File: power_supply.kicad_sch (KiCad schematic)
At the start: 18 parts, among them J1 Разъём к автомобилю 2x16 (32 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, U6 MC78M05CDTG, U7 AMS1117-3.3

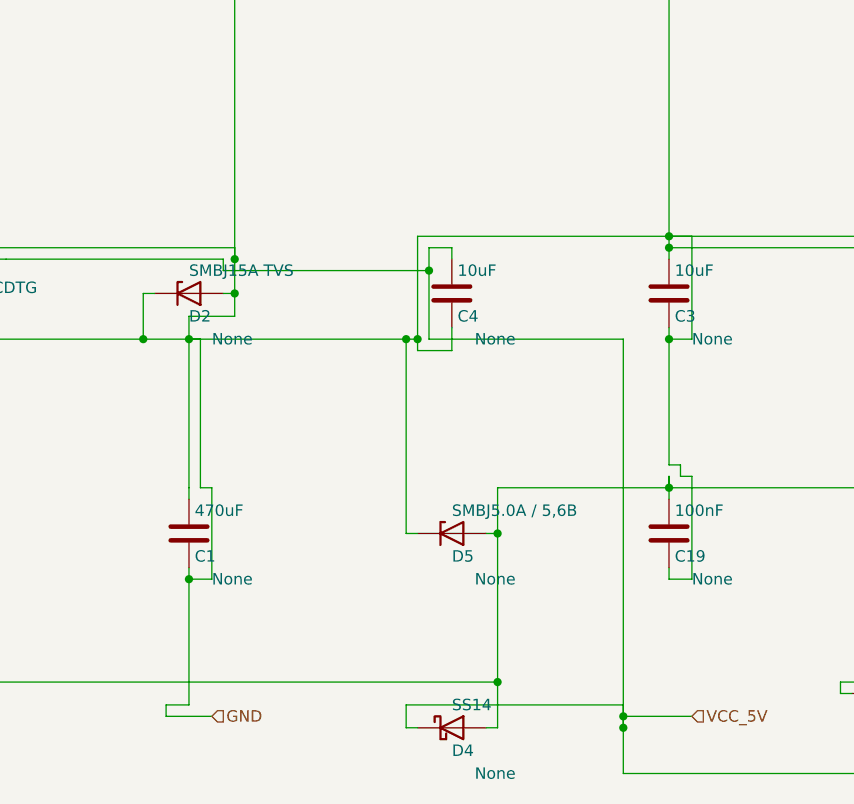
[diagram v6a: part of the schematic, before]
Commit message: фильтр клеток для Т если там пересечение
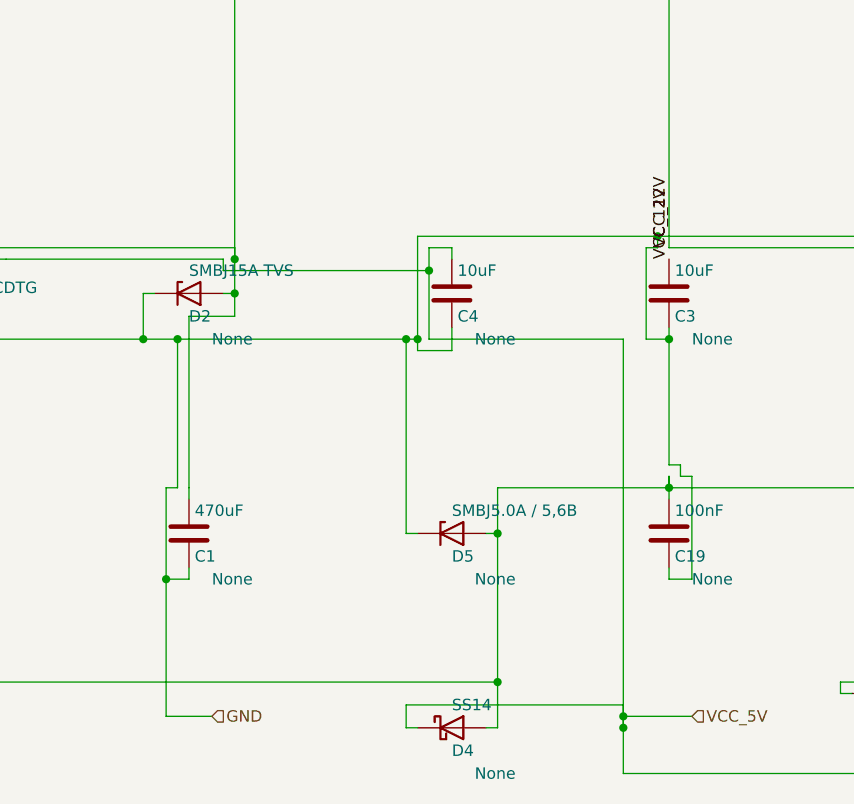
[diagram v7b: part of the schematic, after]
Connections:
- net GND: no longer C1.1, C11.1, C2.1, C20.1, C3.1, D2.2 (A), L1.2, U6.1 (VI)
- new net VCC_12V: C1.1, C11.1, C2.1, C20.1, C3.1, D2.2 (A), L1.2, U6.1 (VI)
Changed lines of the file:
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@@
 		(instances
 			(project "Untitled"
-				(path "/ddde2adb-c5de-407b-b4a5-5687a14e8471"
+				(path "/6a57f7b9-87d0-4bec-9f96-e75792a987b4"
 					(reference "C1")
 					(unit 1)
@@
 		(instances
 			(project "Untitled"
-				(path "/ddde2adb-c5de-407b-b4a5-5687a14e8471"
+				(path "/6a57f7b9-87d0-4bec-9f96-e75792a987b4"
 					(reference "C11")
 					(unit 1)
@@
 		(instances
 			(project "Untitled"
-				(path "/ddde2adb-c5de-407b-b4a5-5687a14e8471"
+				(path "/6a57f7b9-87d0-4bec-9f96-e75792a987b4"
 					(reference "C16")
 					(unit 1)
@@
 		(instances
 			(project "Untitled"
-				(path "/ddde2adb-c5de-407b-b4a5-5687a14e8471"
+				(path "/6a57f7b9-87d0-4bec-9f96-e75792a987b4"
 					(reference "C17")
 					(unit 1)
@@
 		(instances
 			(project "Untitled"
-				(path "/ddde2adb-c5de-407b-b4a5-5687a14e8471"
+				(path "/6a57f7b9-87d0-4bec-9f96-e75792a987b4"
 					(reference "C18")
 					(unit 1)
@@
 		(instances
 			(project "Untitled"
-				(path "/ddde2adb-c5de-407b-b4a5-5687a14e8471"
+				(path "/6a57f7b9-87d0-4bec-9f96-e75792a987b4"
 					(reference "C19")
 					(unit 1)
@@
 		(instances
 			(project "Untitled"
-				(path "/ddde2adb-c5de-407b-b4a5-5687a14e8471"
+				(path "/6a57f7b9-87d0-4bec-9f96-e75792a987b4"
 					(reference "C2")
 					(unit 1)
@@
 		(instances
 			(project "Untitled"
-				(path "/ddde2adb-c5de-407b-b4a5-5687a14e8471"
+				(path "/6a57f7b9-87d0-4bec-9f96-e75792a987b4"
 					(reference "C20")
 					(unit 1)
@@
 		(instances
 			(project "Untitled"
-				(path "/ddde2adb-c5de-407b-b4a5-5687a14e8471"
+				(path "/6a57f7b9-87d0-4bec-9f96-e75792a987b4"
 					(reference "C3")
 					(unit 1)
@@
 		(instances
 			(project "Untitled"
-				(path "/ddde2adb-c5de-407b-b4a5-5687a14e8471"
+				(path "/6a57f7b9-87d0-4bec-9f96-e75792a987b4"
 					(reference "C4")
 					(unit 1)
@@
 		(instances
 			(project "Untitled"
-				(path "/ddde2adb-c5de-407b-b4a5-5687a14e8471"
+				(path "/6a57f7b9-87d0-4bec-9f96-e75792a987b4"
 					(reference "D1")
 					(unit 1)
@@
 		(instances
 			(project "Untitled"
-				(path "/ddde2adb-c5de-407b-b4a5-5687a14e8471"
+				(path "/6a57f7b9-87d0-4bec-9f96-e75792a987b4"
 					(reference "D2")
 					(unit 1)
@@
 		(instances
 			(project "Untitled"
-				(path "/ddde2adb-c5de-407b-b4a5-5687a14e8471"
+				(path "/6a57f7b9-87d0-4bec-9f96-e75792a987b4"
 					(reference "D4")
 					(unit 1)
@@
 		(instances
 			(project "Untitled"
-				(path "/ddde2adb-c5de-407b-b4a5-5687a14e8471"
+				(path "/6a57f7b9-87d0-4bec-9f96-e75792a987b4"
 					(reference "D5")
 					(unit 1)
@@
 		(instances
 			(project "Untitled"
-				(path "/ddde2adb-c5de-407b-b4a5-5687a14e8471"
+				(path "/6a57f7b9-87d0-4bec-9f96-e75792a987b4"
 					(reference "J1")
 					(unit 1)
@@
 		(instances
 			(project "Untitled"
-				(path "/ddde2adb-c5de-407b-b4a5-5687a14e8471"
+				(path "/6a57f7b9-87d0-4bec-9f96-e75792a987b4"
 					(reference "L1")
 					(unit 1)
@@
 		(instances
 			(project "Untitled"
-				(path "/ddde2adb-c5de-407b-b4a5-5687a14e8471"
+				(path "/6a57f7b9-87d0-4bec-9f96-e75792a987b4"
 					(reference "U6")
 					(unit 1)
@@
 		(instances
 			(project "Untitled"
-				(path "/ddde2adb-c5de-407b-b4a5-5687a14e8471"
+				(path "/6a57f7b9-87d0-4bec-9f96-e75792a987b4"
 					(reference "U7")
 					(unit 1)
@@
 	(wire
 		(pts
-			(xy 95.25 130.81) (xy 95.25 129.54)
-		)
-		(stroke
-			(width 0)
-			(type default)
-		)
-	)
-	(wire
-		(pts
 			(xy 3.81 130.81) (xy 2.54 130.81)
 		)
@@
 	(wire
 		(pts
-			(xy 41.91 166.37) (xy 44.45 166.37)
+			(xy 41.91 166.37) (xy 39.37 166.37)
 		)
 		(stroke
@@
 	(wire
 		(pts
-			(xy 44.45 166.37) (xy 44.45 156.21)
+			(xy 39.37 166.37) (xy 39.37 156.21)
 		)
 		(stroke
@@
 	(wire
 		(pts
-			(xy 44.45 156.21) (xy 43.18 156.21)
+			(xy 39.37 156.21) (xy 40.64 156.21)
 		)
 		(stroke
@@
 	(wire
 		(pts
-			(xy 43.18 156.21) (xy 43.18 139.7)
-		)
-		(stroke
-			(width 0)
-			(type default)
-		)
-	)
-	(wire
-		(pts
-			(xy 43.18 139.7) (xy 41.91 139.7)
+			(xy 40.64 156.21) (xy 40.64 139.7)
 		)
 		(stroke
@@
 	(wire
 		(pts
-			(xy 95.25 139.7) (xy 97.79 139.7)
+			(xy 95.25 139.7) (xy 92.71 139.7)
+		)
+		(stroke
+			(width 0)
+			(type default)
+		)
+	)
+	(wire
+		(pts
+			(xy 92.71 139.7) (xy 92.71 129.54)
 		)
 		(stroke
@@
 	(wire
 		(pts
-			(xy 97.79 139.7) (xy 97.79 128.27)
+			(xy 92.71 129.54) (xy 93.98 129.54)
 		)
 		(stroke
@@
 	(wire
 		(pts
-			(xy 97.79 128.27) (xy 95.25 128.27)
+			(xy 93.98 129.54) (xy 93.98 128.27)
 		)
 		(stroke
@@
 	(wire
 		(pts
-			(xy 39.37 181.61) (xy 39.37 180.34)
-		)
-		(stroke
-			(width 0)
-			(type default)
-		)
-	)
-	(wire
-		(pts
-			(xy 39.37 180.34) (xy 41.91 180.34)
-		)
-		(stroke
-			(width 0)
-			(type default)
-		)
-	)
-	(wire
-		(pts
-			(xy 41.91 180.34) (xy 41.91 166.37)
+			(xy 39.37 181.61) (xy 39.37 166.37)
 		)
 		(stroke
@@
 	)
 	(junction
-		(at 95.25 129.54)
-		(diameter 0)
-		(color 0 0 0 0)
-	)
-	(junction
 		(at 46.99 130.81)
 		(diameter 0)
@@
 	)
 	(junction
-		(at 41.91 139.7)
+		(at 40.64 139.7)
 		(diameter 0)
 		(color 0 0 0 0)
@@
 	)
 	(junction
-		(at 95.25 128.27)
+		(at 93.98 128.27)
 		(diameter 0)
 		(color 0 0 0 0)
@@
 	)
 	(junction
-		(at 41.91 166.37)
+		(at 39.37 166.37)
 		(diameter 0)
 		(color 0 0 0 0)
 	)
+	(label "VCC_12V"
+		(at 95.25 130.81 90)
+		(effects
+			(font
+				(size 1.27 1.27)
+			)
+			(justify left bottom)
+		)
+	)
+	(label "VCC_12V"
+		(at 95.25 129.54 90)
+		(effects
+			(font
+				(size 1.27 1.27)
+			)
+			(justify left bottom)
+		)
+	)
 	(hierarchical_label "VCC_12V"

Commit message: fic placer for small schemes
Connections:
- net V5_SENS: now reaches C16.1, C17.1, C18.1, C19.1, D4.2 (A), D5.2 (A), J1.17 (Pin_17)
- net VBAT_IN: now reaches D1.1 (K), J1.1 (Pin_1), J1.2 (Pin_2)
- net VBAT_PROT: now reaches D1.2 (A), L1.1
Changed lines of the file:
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@@
 		(instances
 			(project "Untitled"
-				(path "/6a57f7b9-87d0-4bec-9f96-e75792a987b4"
+				(path "/31b31d6c-a26c-49d6-a21b-feaa7cd09220"
 					(reference "C1")
 					(unit 1)
@@
 		(instances
 			(project "Untitled"
-				(path "/6a57f7b9-87d0-4bec-9f96-e75792a987b4"
+				(path "/31b31d6c-a26c-49d6-a21b-feaa7cd09220"
 					(reference "C11")
 					(unit 1)
@@
 		(instances
 			(project "Untitled"
-				(path "/6a57f7b9-87d0-4bec-9f96-e75792a987b4"
+				(path "/31b31d6c-a26c-49d6-a21b-feaa7cd09220"
 					(reference "C16")
 					(unit 1)
@@
 		(instances
 			(project "Untitled"
-				(path "/6a57f7b9-87d0-4bec-9f96-e75792a987b4"
+				(path "/31b31d6c-a26c-49d6-a21b-feaa7cd09220"
 					(reference "C17")
 					(unit 1)
@@
 		(instances
 			(project "Untitled"
-				(path "/6a57f7b9-87d0-4bec-9f96-e75792a987b4"
+				(path "/31b31d6c-a26c-49d6-a21b-feaa7cd09220"
 					(reference "C18")
 					(unit 1)
@@
 		(instances
 			(project "Untitled"
-				(path "/6a57f7b9-87d0-4bec-9f96-e75792a987b4"
+				(path "/31b31d6c-a26c-49d6-a21b-feaa7cd09220"
 					(reference "C19")
 					(unit 1)
@@
 		(instances
 			(project "Untitled"
-				(path "/6a57f7b9-87d0-4bec-9f96-e75792a987b4"
+				(path "/31b31d6c-a26c-49d6-a21b-feaa7cd09220"
 					(reference "C2")
 					(unit 1)
@@
 		(instances
 			(project "Untitled"
-				(path "/6a57f7b9-87d0-4bec-9f96-e75792a987b4"
+				(path "/31b31d6c-a26c-49d6-a21b-feaa7cd09220"
 					(reference "C20")
 					(unit 1)
@@
 		(instances
 			(project "Untitled"
-				(path "/6a57f7b9-87d0-4bec-9f96-e75792a987b4"
+				(path "/31b31d6c-a26c-49d6-a21b-feaa7cd09220"
 					(reference "C3")
 					(unit 1)
@@
 		(instances
 			(project "Untitled"
-				(path "/6a57f7b9-87d0-4bec-9f96-e75792a987b4"
+				(path "/31b31d6c-a26c-49d6-a21b-feaa7cd09220"
 					(reference "C4")
 					(unit 1)
@@
 		(instances
 			(project "Untitled"
-				(path "/6a57f7b9-87d0-4bec-9f96-e75792a987b4"
+				(path "/31b31d6c-a26c-49d6-a21b-feaa7cd09220"
 					(reference "D1")
 					(unit 1)
@@
 		(instances
 			(project "Untitled"
-				(path "/6a57f7b9-87d0-4bec-9f96-e75792a987b4"
+				(path "/31b31d6c-a26c-49d6-a21b-feaa7cd09220"
 					(reference "D2")
 					(unit 1)
@@
 		(instances
 			(project "Untitled"
-				(path "/6a57f7b9-87d0-4bec-9f96-e75792a987b4"
+				(path "/31b31d6c-a26c-49d6-a21b-feaa7cd09220"
 					(reference "D4")
 					(unit 1)
@@
 		(instances
 			(project "Untitled"
-				(path "/6a57f7b9-87d0-4bec-9f96-e75792a987b4"
+				(path "/31b31d6c-a26c-49d6-a21b-feaa7cd09220"
 					(reference "D5")
 					(unit 1)
@@
 		(instances
 			(project "Untitled"
-				(path "/6a57f7b9-87d0-4bec-9f96-e75792a987b4"
+				(path "/31b31d6c-a26c-49d6-a21b-feaa7cd09220"
 					(reference "J1")
 					(unit 1)
@@
 		(instances
 			(project "Untitled"
-				(path "/6a57f7b9-87d0-4bec-9f96-e75792a987b4"
+				(path "/31b31d6c-a26c-49d6-a21b-feaa7cd09220"
 					(reference "L1")
 					(unit 1)
@@
 		(instances
 			(project "Untitled"
-				(path "/6a57f7b9-87d0-4bec-9f96-e75792a987b4"
+				(path "/31b31d6c-a26c-49d6-a21b-feaa7cd09220"
 					(reference "U6")
 					(unit 1)
@@
 		(instances
 			(project "Untitled"
-				(path "/6a57f7b9-87d0-4bec-9f96-e75792a987b4"
+				(path "/31b31d6c-a26c-49d6-a21b-feaa7cd09220"
 					(reference "U7")
 					(unit 1)
@@
 		(effects
 			(font
+				(size 1.27 1.27)
+			)
+			(justify left bottom)
+		)
+	)
+	(label "VBAT_IN"
+		(at 6.35 6.35 90)
+		(effects
+			(font
+				(size 1.27 1.27)
+			)
+			(justify left bottom)
+		)
+	)
+	(label "VBAT_PROT"
+		(at 25.4 5.08 0.0000)
+		(effects
+			(font
+				(size 1.27 1.27)
+			)
+			(justify left bottom)
+		)
+	)
+	(label "V5_SENS"
+		(at 124.46 156.21 0.0000)
+		(effects
+			(font
